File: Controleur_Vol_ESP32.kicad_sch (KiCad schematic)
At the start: 63 parts, among them J1 Conn_01x03, J10 Conn_01x03, J11 Conn_01x08, J12 Conn_01x03, J13 Conn_01x03, J2 Conn_01x03, J3 Conn_01x03, J4 Conn_01x03, J5 Conn_01x03, J6 Conn_01x03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

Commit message: Ajout composants manquants sur schéma Assignation empreintes à tous les composants Ajout composant ESP32-devkit-v1 au projet
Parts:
- removed JP1: SolderJumper_2_Open, symbol Jumper:SolderJumper_2_Open
- removed U2: LD1117S33TR_SOT223, Package_TO_SOT_SMD:SOT-223-3_TabPin2, symbol Regulator_Linear:LD1117S33TR_SOT223
- added C23: 10nF, Capacitor_SMD:C_1206_3216Metric_Pad1.33x1.80mm_HandSolder, symbol Device:C
- added C24: 100µF, Capacitor_Tantalum_SMD:CP_EIA-6032-20_AVX-F_Pad2.25x2.35mm_HandSolder, symbol Device:C_Polarized
- added J14: Conn_01x04, Connector_PinHeader_2.54mm:PinHeader_1x04_P2.54mm_Vertical, symbol Connector_Generic:Conn_01x04
- added J15: Screw_Terminal_01x02, TerminalBlock:TerminalBlock_bornier-2_P5.08mm, symbol Connector:Screw_Terminal_01x02
- added JP1, JP2: Jumper_2_Open, Connector_PinHeader_2.54mm:PinHeader_1x02_P2.54mm_Vertical, symbol Jumper:Jumper_2_Open
- J10, J12, J13, J7, J8, J9: footprint (none) -> Connector_PinHeader_2.54mm:PinHeader_1x03_P2.54mm_Vertical
- J11: footprint (none) -> Connector_PinHeader_2.54mm:PinHeader_1x08_P2.54mm_Vertical
- U1: footprint Personal:esp32_devkit_v1_doit -> esp32-devkit-v1:esp32_devkit_v1_doit
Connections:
- net +3.3V: now also J14.1 (Pin_1); no longer C19.1
- net +5V: now also C19.1, U3.1 (OUT), JP1.2 (B); no longer C18.1, C20.2, U4.1 (+V)
- net GND: now also U3.2 (GND), U3.3 (GND), U3.6 (GND), U3.7 (GND), C23.1, C24.2, J14.4 (Pin_4), J15.2 (Pin_2)
- net SCL: now also J14.3 (Pin_3)
- net SDA: now also J14.2 (Pin_2)
- net VBATT: now also C23.2
- net +VIN: now reaches U3.8 (IN)
- net +VIN: now also C18.1, C20.2, U4.1 (+V), C24.1, JP1.1 (A), JP2.1 (A)
- net at R19.2: now also J15.1 (Pin_1), JP2.2 (B)
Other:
- moved on the sheet: R19, R20, U3

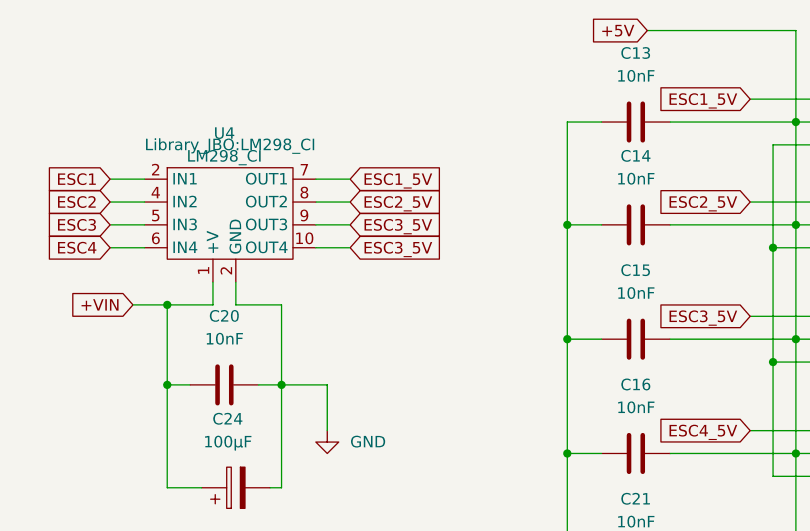
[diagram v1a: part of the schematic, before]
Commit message: Correction erreurs liens
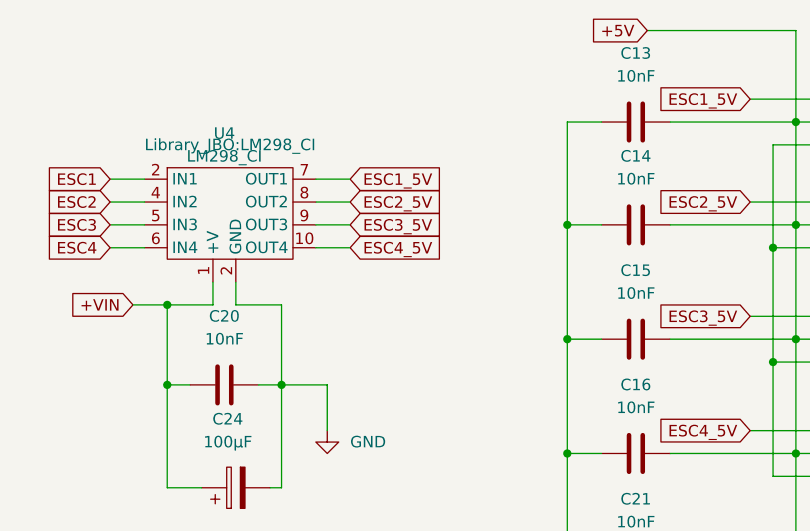
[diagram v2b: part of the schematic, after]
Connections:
- net ESC3_5V: no longer U4.10 (OUT4)
- net ESC4_5V: now also U4.10 (OUT4)
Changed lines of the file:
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@@
     )
   )
-  (global_label "ESC3_5V" (shape input) (at 212.09 39.37 0) (fields_autoplaced)
+  (global_label "ESC4_5V" (shape input) (at 212.09 39.37 0) (fields_autoplaced)
     (effects (font (size 1.27 1.27)) (justify left))
     (property "Références Inter-Feuilles" "${INTERSHEET_REFS}" (id 0) (at 222.6069 39.2906 0)

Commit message: Ajout données cartouche
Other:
- company: (none) -> Bocal Chemillé
- title: (none) -> Controleur Vol ESP32
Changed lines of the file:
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@@
 (kicad_sch (version 20211123) (generator eeschema)
   (paper "A4")
+  (title_block
+    (title "Controleur Vol ESP32")
+    (date "2022-12-23")
+    (rev "1.0.0")
+    (company "Bocal Chemillé")
+  )
   (junction (at 52.07 97.79) (diameter 0) (color 0 0 0 0)
   )

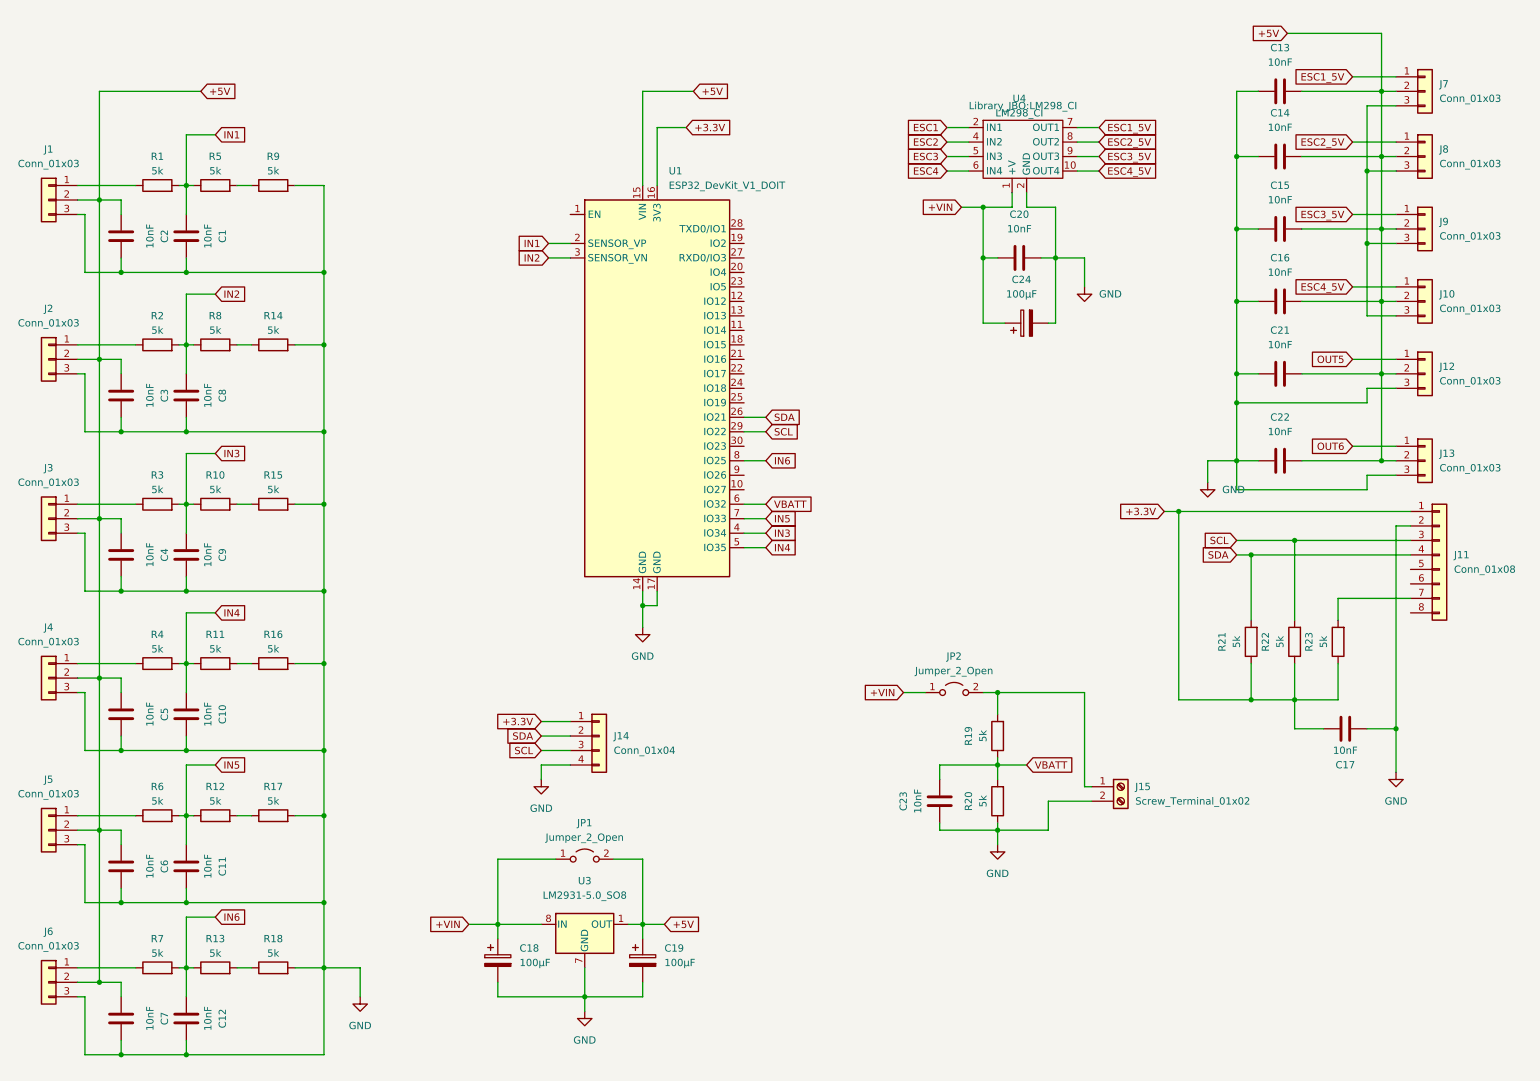
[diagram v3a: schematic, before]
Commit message: Simplification schéma + MAJ lib symboles/empreintes
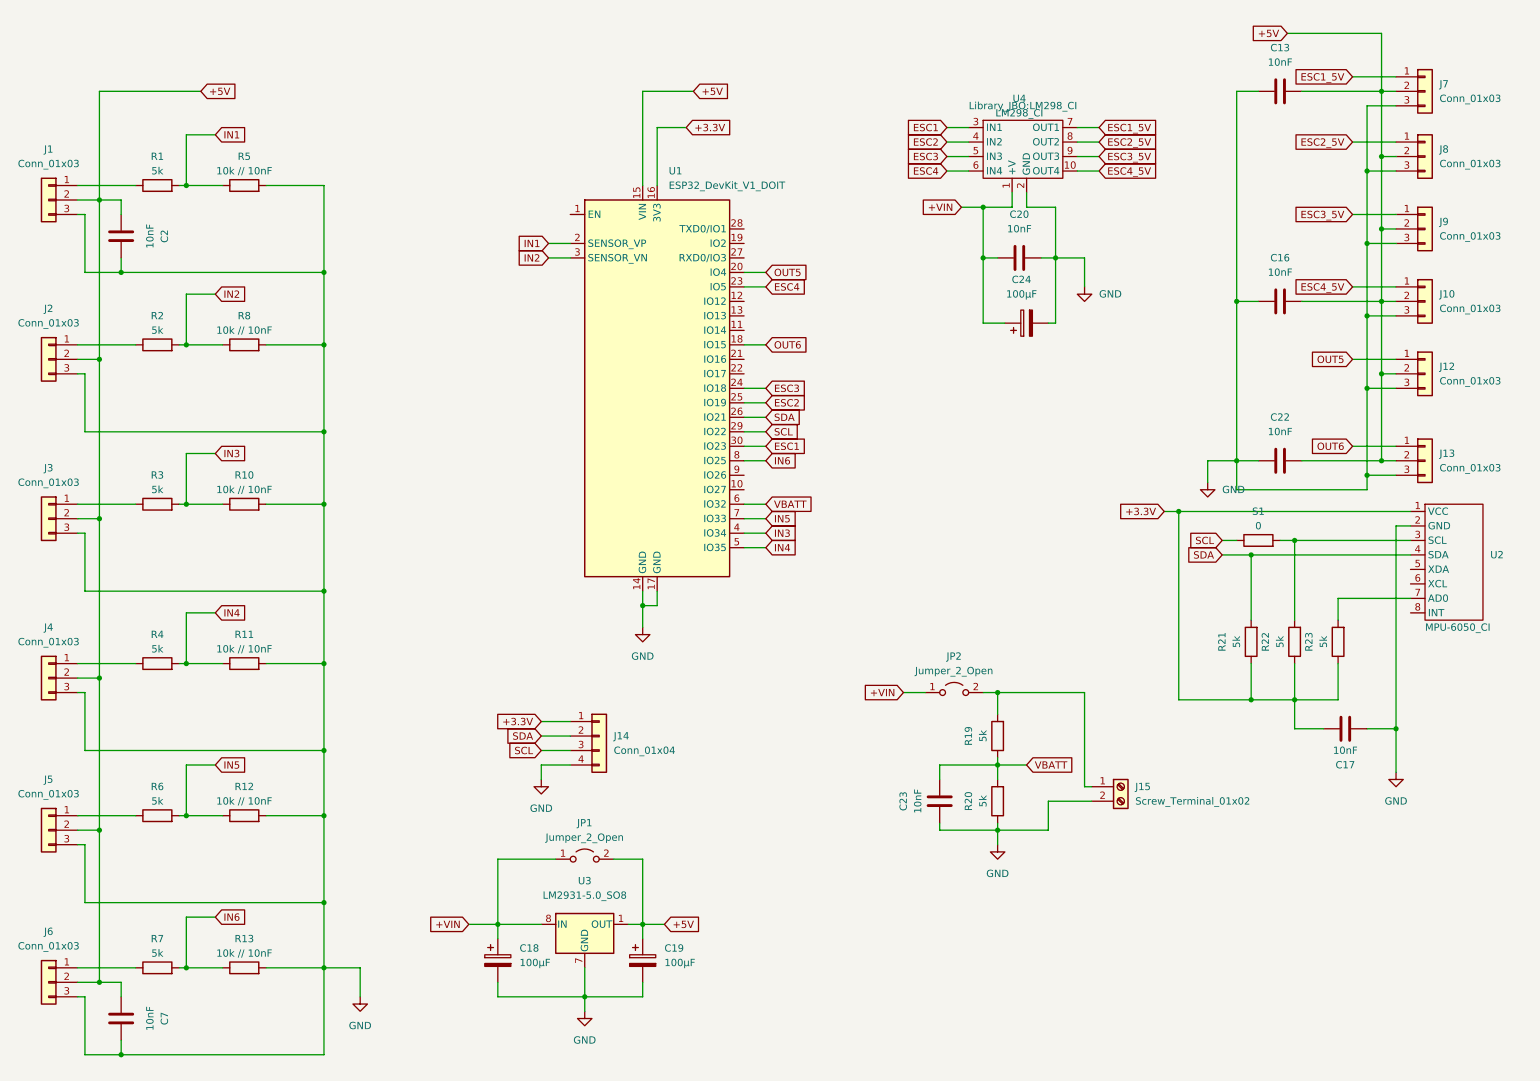
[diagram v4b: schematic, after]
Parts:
- removed C1, C10, C11, C12, C14, C15, C21, C3, C4, C5, C6, C8, C9: 10nF, Capacitor_SMD:C_1206_3216Metric_Pad1.33x1.80mm_HandSolder, symbol Device:C
- removed J11: Conn_01x08, Connector_PinHeader_2.54mm:PinHeader_1x08_P2.54mm_Vertical, symbol Connector_Generic:Conn_01x08
- removed R14, R15, R16, R17, R18, R9: 5k, Resistor_SMD:R_1206_3216Metric_Pad1.30x1.75mm_HandSolder, symbol Device:R
- added S1: 0, Resistor_SMD:R_1206_3216Metric_Pad1.30x1.75mm_HandSolder, symbol Device:R
- added U2: MPU-6050_CI, Library_JBO:MPU-6050_CI, symbol Project_Lib:MPU-6050_CI
- R10, R11, R12, R13, R5, R8: value 5k -> 10k // 10nF
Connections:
- net +3.3V: now also U2.1 (VCC)
- net ESC1: now also U1.30 (IO23), U4.3 (IN1); no longer U4.2 (IN1)
- net ESC2: now also U1.25 (IO19)
- net ESC3: now also U1.24 (IO18)
- net ESC4: now also U1.23 (IO5)
- net GND: now also J10.3 (Pin_3), J7.3 (Pin_3), J8.3 (Pin_3), J9.3 (Pin_3), R10.2, R11.2, R12.2, R13.2, R5.2, R8.2, U2.2 (GND)
- net OUT5: now also U1.20 (IO4)
- net OUT6: now also U1.18 (IO15)
- net SCL: now also S1.1; no longer R22.2
- net SDA: now also U2.4 (SDA)
- net at R23.2: now also U2.7 (AD0)
- new net: R22.2, S1.2, U2.3 (SCL)
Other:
- moved on the sheet: R10, R11, R12, R13, R5, R8

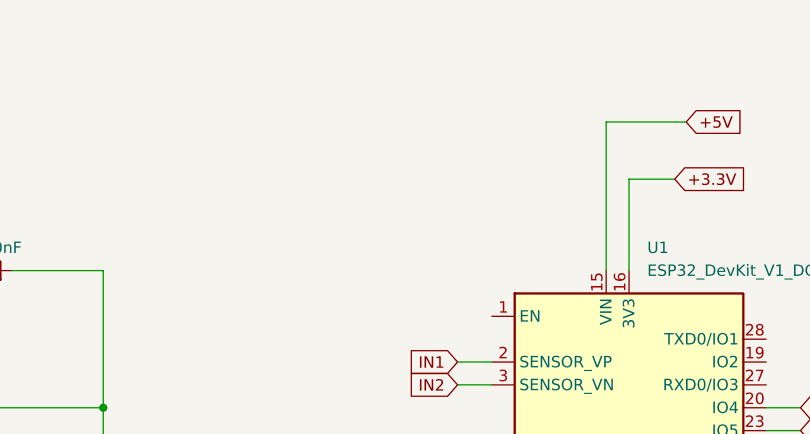
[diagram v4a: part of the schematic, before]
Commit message: Ajout trous de fixation
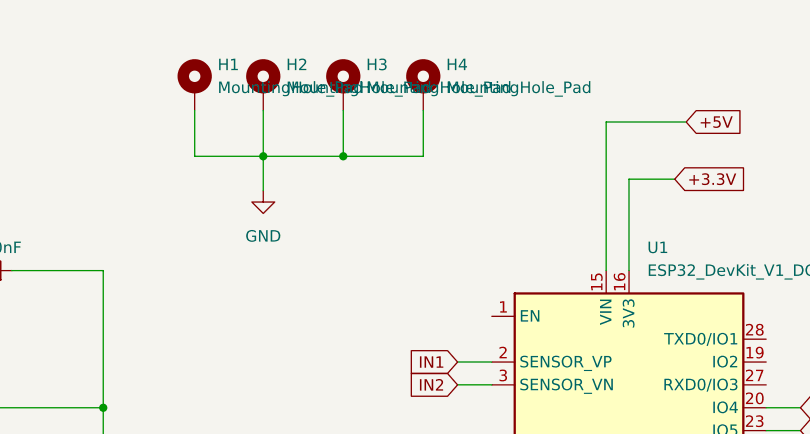
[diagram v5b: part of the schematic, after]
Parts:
- added H1, H2, H3, H4: MountingHole_Pad, MountingHole:MountingHole_4.3mm_M4, symbol Mechanical:MountingHole_Pad
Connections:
- net GND: now also H1.1, H2.1, H3.1, H4.1
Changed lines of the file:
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@@
   (junction (at 76.2 69.85) (diameter 0) (color 0 0 0 0)
   )
+  (junction (at 93.98 29.21) (diameter 0) (color 0 0 0 0)
+  )
   (junction (at 246.38 132.08) (diameter 0) (color 0 0 0 0)
   )
@@
   (junction (at 76.2 140.97) (diameter 0) (color 0 0 0 0)
   )
+  (junction (at 102.87 29.21) (diameter 0) (color 0 0 0 0)
+  )
   (junction (at 52.07 69.85) (diameter 0) (color 0 0 0 0)
   )
@@
     (stroke (width 0) (type default) (color 0 0 0 0))
   )
+  (wire (pts (xy 93.98 29.21) (xy 93.98 33.02))
+    (stroke (width 0) (type default) (color 0 0 0 0))
+  )
   (wire (pts (xy 247.65 62.23) (xy 261.62 62.23))
     (stroke (width 0) (type default) (color 0 0 0 0))
@@
     (stroke (width 0) (type default) (color 0 0 0 0))
   )
+  (wire (pts (xy 93.98 24.13) (xy 93.98 29.21))
+    (stroke (width 0) (type default) (color 0 0 0 0))
+  )
   (wire (pts (xy 209.55 130.81) (xy 209.55 147.32))
     (stroke (width 0) (type default) (color 0 0 0 0))
@@
     (stroke (width 0) (type default) (color 0 0 0 0))
   )
+  (wire (pts (xy 86.36 29.21) (xy 93.98 29.21))
+    (stroke (width 0) (type default) (color 0 0 0 0))
+  )
   (wire (pts (xy 82.55 184.15) (xy 82.55 179.07))
     (stroke (width 0) (type default) (color 0 0 0 0))
@@
     (stroke (width 0) (type default) (color 0 0 0 0))
   )
+  (wire (pts (xy 102.87 29.21) (xy 111.76 29.21))
+    (stroke (width 0) (type default) (color 0 0 0 0))
+  )
   (wire (pts (xy 256.54 87.63) (xy 264.16 87.63))
     (stroke (width 0) (type default) (color 0 0 0 0))
@@
     (stroke (width 0) (type default) (color 0 0 0 0))
   )
+  (wire (pts (xy 93.98 29.21) (xy 102.87 29.21))
+    (stroke (width 0) (type default) (color 0 0 0 0))
+  )
   (wire (pts (xy 204.47 54.61) (xy 204.47 66.04))
     (stroke (width 0) (type default) (color 0 0 0 0))
@@
     (stroke (width 0) (type default) (color 0 0 0 0))
   )
+  (wire (pts (xy 86.36 24.13) (xy 86.36 29.21))
+    (stroke (width 0) (type default) (color 0 0 0 0))
+  )
   (wire (pts (xy 132.08 41.91) (xy 132.08 25.4))
     (stroke (width 0) (type default) (color 0 0 0 0))
@@
     (stroke (width 0) (type default) (color 0 0 0 0))
   )
+  (wire (pts (xy 111.76 24.13) (xy 111.76 29.21))
+    (stroke (width 0) (type default) (color 0 0 0 0))
+  )
   (wire (pts (xy 238.76 106.68) (xy 238.76 118.11))
     (stroke (width 0) (type default) (color 0 0 0 0))
@@
   )
   (wire (pts (xy 203.2 149.86) (xy 203.2 154.94))
+    (stroke (width 0) (type default) (color 0 0 0 0))
+  )
+  (wire (pts (xy 102.87 24.13) (xy 102.87 29.21))
     (stroke (width 0) (type default) (color 0 0 0 0))
   )
@@
     (pin "3")
   )
+  (symbol (lib_id "Mechanical:MountingHole_Pad") (at 102.87 21.59 0) (unit 1)
+    (in_bom yes) (on_board yes) (fields_autoplaced)
+    (property "Reference" "H3" (id 0) (at 105.41 19.0499 0)
+      (effects (font (size 1.27 1.27)) (justify left))
+    )
+    (property "Value" "MountingHole_Pad" (id 1) (at 105.41 21.5899 0)
+      (effects (font (size 1.27 1.27)) (justify left))
+    )
+    (property "Footprint" "MountingHole:MountingHole_4.3mm_M4" (id 2) (at 102.87 21.59 0)
+      (effects (font (size 1.27 1.27)) hide)
+    )
+    (property "Datasheet" "~" (id 3) (at 102.87 21.59 0)
+      (effects (font (size 1.27 1.27)) hide)
+    )
+    (pin "1")
+  )
   (symbol (lib_id "power:GND") (at 264.16 144.78 0) (unit 1)
     (in_bom yes) (on_board yes) (fields_autoplaced)
@@
     (pin "1")
     (pin "2")
+  )
+  (symbol (lib_id "Mechanical:MountingHole_Pad") (at 93.98 21.59 0) (unit 1)
+    (in_bom yes) (on_board yes) (fields_autoplaced)
+    (property "Reference" "H2" (id 0) (at 96.52 19.0499 0)
+      (effects (font (size 1.27 1.27)) (justify left))
+    )
+    (property "Value" "MountingHole_Pad" (id 1) (at 96.52 21.5899 0)
+      (effects (font (size 1.27 1.27)) (justify left))
+    )
+    (property "Footprint" "MountingHole:MountingHole_4.3mm_M4" (id 2) (at 93.98 21.59 0)
+      (effects (font (size 1.27 1.27)) hide)
+    )
+    (property "Datasheet" "~" (id 3) (at 93.98 21.59 0)
+      (effects (font (size 1.27 1.27)) hide)
+    )
+    (pin "1")
   )
   (symbol (lib_id "Device:R") (at 194.31 138.43 180) (unit 1)
@@
     (pin "3")
   )
+  (symbol (lib_id "Mechanical:MountingHole_Pad") (at 111.76 21.59 0) (unit 1)
+    (in_bom yes) (on_board yes) (fields_autoplaced)
+    (property "Reference" "H4" (id 0) (at 114.3 19.0499 0)
+      (effects (font (size 1.27 1.27)) (justify left))
+    )
+    (property "Value" "MountingHole_Pad" (id 1) (at 114.3 21.5899 0)
+      (effects (font (size 1.27 1.27)) (justify left))
+    )
+    (property "Footprint" "MountingHole:MountingHole_4.3mm_M4" (id 2) (at 111.76 21.59 0)
+      (effects (font (size 1.27 1.27)) hide)
+    )
+    (property "Datasheet" "~" (id 3) (at 111.76 21.59 0)
+      (effects (font (size 1.27 1.27)) hide)
+    )
+    (pin "1")
+  )
   (symbol (lib_id "Connector_Generic:Conn_01x03") (at 269.24 90.17 0) (unit 1)
     (in_bom yes) (on_board yes) (fields_autoplaced)
@@
     (pin "2")
   )
+  (symbol (lib_id "power:GND") (at 93.98 33.02 0) (unit 1)
+    (in_bom yes) (on_board yes) (fields_autoplaced)
+    (property "Reference" "#PWR0104" (id 0) (at 93.98 39.37 0)
+      (effects (font (size 1.27 1.27)) hide)
+    )
+    (property "Value" "GND" (id 1) (at 93.98 38.1 0))
+    (property "Footprint" "" (id 2) (at 93.98 33.02 0)
+      (effects (font (size 1.27 1.27)) hide)
+    )
+    (property "Datasheet" "" (id 3) (at 93.98 33.02 0)
+      (effects (font (size 1.27 1.27)) hide)
+    )
+    (pin "1")
+  )
   (symbol (lib_id "Device:R") (at 194.31 149.86 180) (unit 1)
     (in_bom yes) (on_board yes)
@@
     (pin "2")
   )
+  (symbol (lib_id "Mechanical:MountingHole_Pad") (at 86.36 21.59 0) (unit 1)
+    (in_bom yes) (on_board yes) (fields_autoplaced)
+    (property "Reference" "H1" (id 0) (at 88.9 19.0499 0)
+      (effects (font (size 1.27 1.27)) (justify left))
+    )
+    (property "Value" "MountingHole_Pad" (id 1) (at 88.9 21.5899 0)
+      (effects (font (size 1.27 1.27)) (justify left))
+    )
+    (property "Footprint" "MountingHole:MountingHole_4.3mm_M4" (id 2) (at 86.36 21.59 0)
+      (effects (font (size 1.27 1.27)) hide)
+    )
+    (property "Datasheet" "~" (id 3) (at 86.36 21.59 0)
+      (effects (font (size 1.27 1.27)) hide)
+    )
+    (pin "1")
+  )
   (symbol (lib_id "Connector_Generic:Conn_01x03") (at 269.24 74.93 0) (unit 1)
     (in_bom yes) (on_board yes) (fields_autoplaced)
@@
       (reference "#PWR0103") (unit 1) (value "GND") (footprint "")
     )
+    (path "/c420888e-4e15-4bf8-993d-7b7a296534b4"
+      (reference "#PWR0104") (unit 1) (value "GND") (footprint "")
+    )
     (path "/60e65266-cd48-4435-ac8c-828b350a1925"
       (reference "C2") (unit 1) (value "10nF") (footprint "Capacitor_SMD:C_1206_3216Metric_Pad1.33x1.80mm_HandSolder")
@@
       (reference "C24") (unit 1) (value "100µF") (footprint "Capacitor_Tantalum_SMD:CP_EIA-6032-20_AVX-F_Pad2.25x2.35mm_HandSolder")
     )
+    (path "/ddb5aff9-5979-41ff-b396-ca43905754d3"
+      (reference "H1") (unit 1) (value "MountingHole_Pad") (footprint "MountingHole:MountingHole_4.3mm_M4")
+    )
+    (path "/5d9dbeb0-ab9f-49f8-9adc-1bc1bcc5b9a8"
+      (reference "H2") (unit 1) (value "MountingHole_Pad") (footprint "MountingHole:MountingHole_4.3mm_M4")
+    )
+    (path "/30edd65c-3235-43c5-9ea4-083ad92c9819"
+      (reference "H3") (unit 1) (value "MountingHole_Pad") (footprint "MountingHole:MountingHole_4.3mm_M4")
+    )
+    (path "/ba66ef92-2bab-4308-ba2c-e8da2f59050e"
+      (reference "H4") (unit 1) (value "MountingHole_Pad") (footprint "MountingHole:MountingHole_4.3mm_M4")
+    )
     (path "/d55057e1-a230-4eae-9783-016981f1484a"
